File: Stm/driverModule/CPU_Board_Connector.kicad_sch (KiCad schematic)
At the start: 1 part, among them J2 2041119-1 (Mini Pcie Express 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

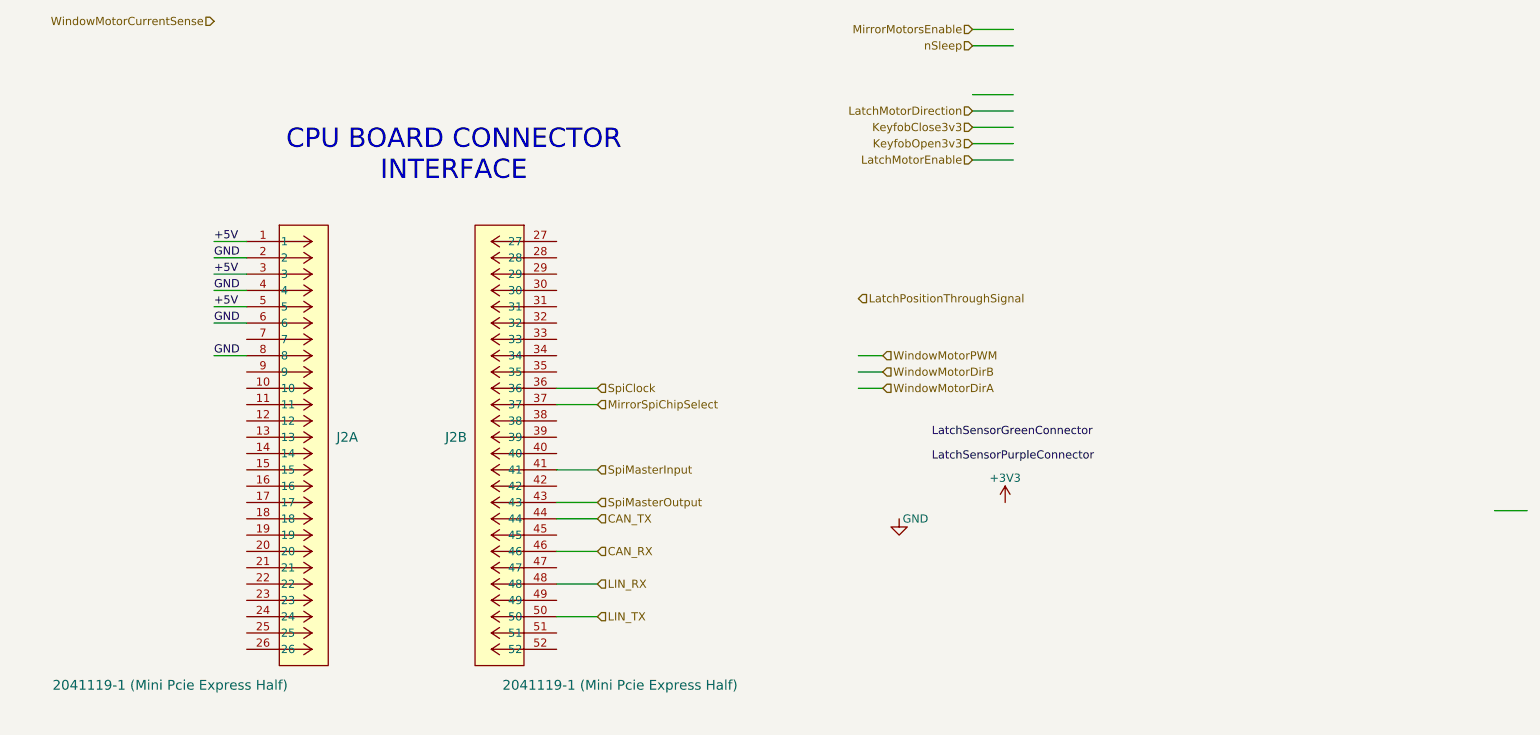
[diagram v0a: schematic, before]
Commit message: Connector
Connect all missing inputs and outputs
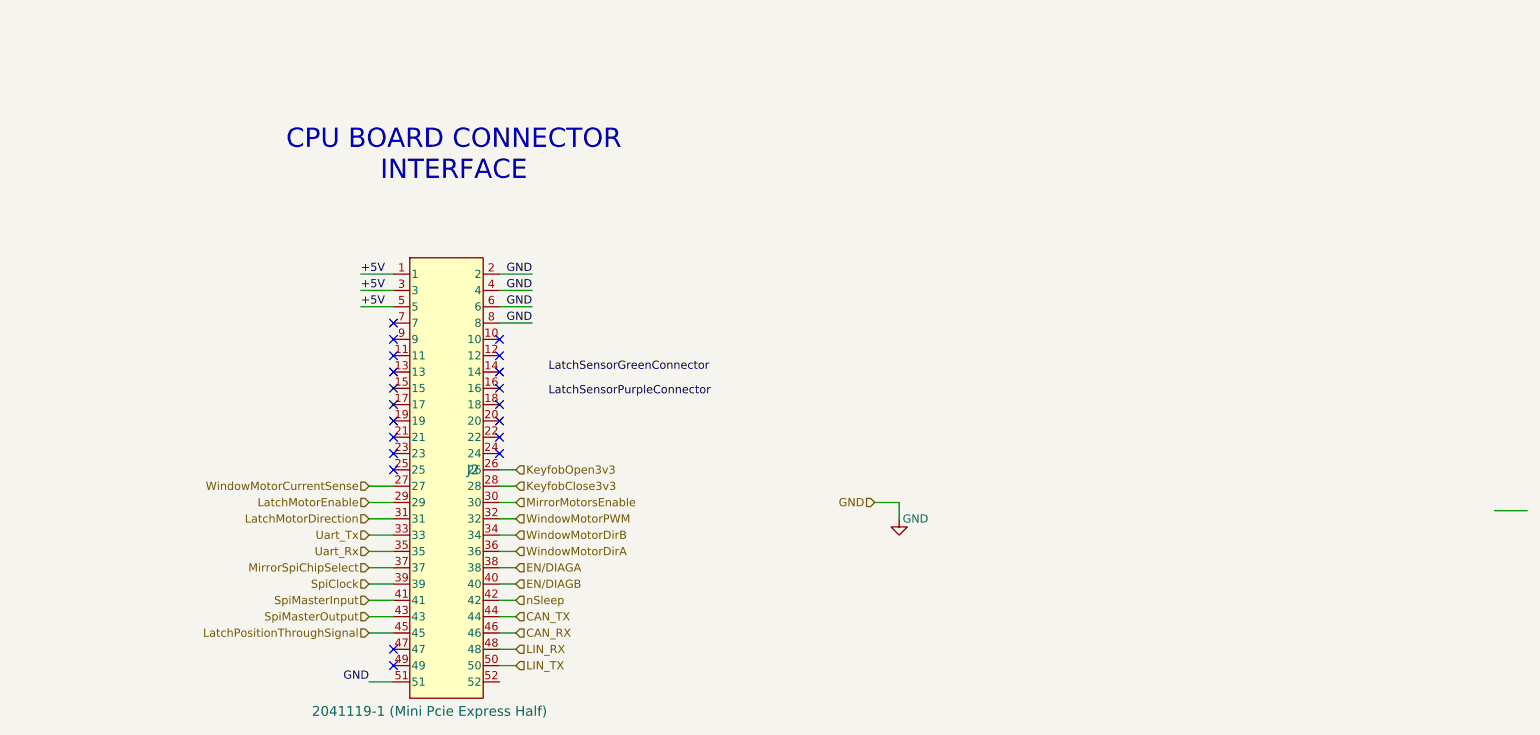
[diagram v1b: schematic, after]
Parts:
- removed unit 2 of J2
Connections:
- net CAN_RX: now also J2.46
- net CAN_TX: now also J2.44
- net GND: now also J2.51
- net KeyfobClose3v3: now also J2.28
- net KeyfobOpen3v3: now also J2.26
- net LIN_RX: now also J2.48
- net LIN_TX: now also J2.50
- net LatchMotorDirection: now also J2.31
- net LatchMotorEnable: now also J2.29
- net LatchPositionThroughSignal: now also J2.45
- net MirrorMotorsEnable: now also J2.30
- net MirrorSpiChipSelect: now also J2.37
- net SpiClock: now also J2.39
- net SpiMasterInput: now also J2.41
- net SpiMasterOutput: now also J2.43
- net WindowMotorCurrentSense: now also J2.27
- net WindowMotorDirA: now also J2.36
- net WindowMotorDirB: now also J2.34
- net WindowMotorPWM: now also J2.32
- net nSleep: now also J2.42
- new net EN/DIAGA: J2.38
- new net EN/DIAGB: J2.40
- new net Uart_Rx: J2.35
- new net Uart_Tx: J2.33
- no-connect marks 0 -> 20
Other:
- moved on the sheet: J2

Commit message: Connectors
Remove some enable signals
Added Harness connectors
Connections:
- net EN/DIAGB is gone; now on net LatchSensorGreenConnector: J2.40
- net nSleep is gone; now on net LatchSensorPurpleConnector: J2.42
- net EN/DIAGA renamed WindownMotorEnable
- net MirrorMotorsEnable: no longer names the net of J2.30
- net WindowMotorDirA renamed WindowMotorDir
- net WindowMotorDirB: no longer names the net of J2.34
- net WindowMotorPWM: no longer names the net of J2.32
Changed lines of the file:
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@@
-	(wire
-		(pts
-			(xy 148.59 101.6) (xy 151.13 101.6)
-		)
-		(stroke
-			(width 0)
-			(type default)
-		)
-	)
 	(wire
 		(pts
@@
 	(wire
 		(pts
-			(xy 148.59 106.68) (xy 151.13 106.68)
-		)
-		(stroke
-			(width 0)
-			(type default)
-		)
-	)
-	(wire
-		(pts
 			(xy 153.67 68.58) (xy 148.59 68.58)
 		)
@@
 	(wire
 		(pts
-			(xy 148.59 104.14) (xy 151.13 104.14)
-		)
-		(stroke
-			(width 0)
-			(type default)
-		)
-	)
-	(wire
-		(pts
 			(xy 148.59 99.06) (xy 151.13 99.06)
 		)
@@
 			(width 0)
 			(type default)
-		)
-	)
-	(label "LatchSensorPurpleConnector"
-		(at 156.21 85.09 0)
-		(effects
-			(font
-				(size 1.27 1.27)
-			)
-			(justify left bottom)
 		)
 	)
@@
 		)
 	)
-	(label "LatchSensorGreenConnector"
-		(at 156.21 81.28 0)
-		(effects
-			(font
-				(size 1.27 1.27)
-			)
-			(justify left bottom)
-		)
-	)
 	(label "GND"
 		(at 153.67 66.04 180)
@@
 		)
 	)
-	(hierarchical_label "WindowMotorPWM"
-		(shape input)
-		(at 151.13 104.14 0)
-		(effects
-			(font
-				(size 1.27 1.27)
-			)
-			(justify left)
-		)
-	)
 	(hierarchical_label "Uart_Rx"
 		(shape input)
@@
 		)
 	)
-	(hierarchical_label "MirrorMotorsEnable"
-		(shape input)
-		(at 151.13 101.6 0)
-		(effects
-			(font
-				(size 1.27 1.27)
-			)
-			(justify left)
-		)
-	)
 	(hierarchical_label "KeyfobClose3v3"
 		(shape input)
@@
 		)
 	)
-	(hierarchical_label "WindowMotorDirA"
+	(hierarchical_label "WindowMotorDir"
 		(shape input)
 		(at 151.13 109.22 0)
@@
 		)
 	)
+	(hierarchical_label "LatchSensorPurpleConnector"
+		(shape input)
+		(at 151.13 116.84 0)
+		(effects
+			(font
+				(size 1.27 1.27)
+			)
+			(justify left)
+		)
+	)
+	(hierarchical_label "WindownMotorEnable"
+		(shape input)
+		(at 151.13 111.76 0)
+		(effects
+			(font
+				(size 1.27 1.27)
+			)
+			(justify left)
+		)
+	)
 	(hierarchical_label "CAN_TX"
 		(shape input)
@@
 		)
 	)
-	(hierarchical_label "WindowMotorDirB"
-		(shape input)
-		(at 151.13 106.68 0)
-		(effects
-			(font
-				(size 1.27 1.27)
-			)
-			(justify left)
-		)
-	)
 	(hierarchical_label "SpiMasterOutput"
 		(shape input)
@@
 		)
 	)
-	(hierarchical_label "nSleep"
-		(shape input)
-		(at 151.13 116.84 0)
+	(hierarchical_label "LatchSensorGreenConnector"
+		(shape input)
+		(at 151.13 114.3 0)
 		(effects
 			(font
@@
 		)
 	)
-	(hierarchical_label "EN{slash}DIAGB"
-		(shape input)
-		(at 151.13 114.3 0)
-		(effects
-			(font
-				(size 1.27 1.27)
-			)
-			(justify left)
-		)
-	)
-	(hierarchical_label "EN{slash}DIAGA"
-		(shape input)
-		(at 151.13 111.76 0)
-		(effects
-			(font
-				(size 1.27 1.27)
-			)
-			(justify left)
-		)
-	)

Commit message: routing
Finished PCB routing
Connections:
- no-connect marks 20 -> 24

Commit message: ADC
Added adc to read passenger input signals
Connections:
- net LatchMotorEnable: now also J2.36; no longer J2.29
- net WindowMotorCurrentSense: now also J2.29; no longer J2.27
- net WindowMotorDir: now also J2.32; no longer J2.36
- net WindowMotorEnable: now reaches J2.34
- net ~{pdrst1}: now reaches J2.52
- net WindownMotorEnable renamed ~{pdrst2}
- no-connect marks 24 -> 22
